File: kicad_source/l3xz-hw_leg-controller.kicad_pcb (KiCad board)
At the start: 2 copper layers, 178 x 29 mm, 57 parts, among them CN1 ARDUINO_NANO_33, CN2 SM04B-SRSS-TB, CN3 SM04B-SRSS-TB, CN4 GH_SM04B-GHS-TB, CN5 GH_SM04B-GHS-TB, CN6 691322310002, CN7 CONN_02X03, CN8 691382010002, U1 AS5048A, U2 AS5048A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

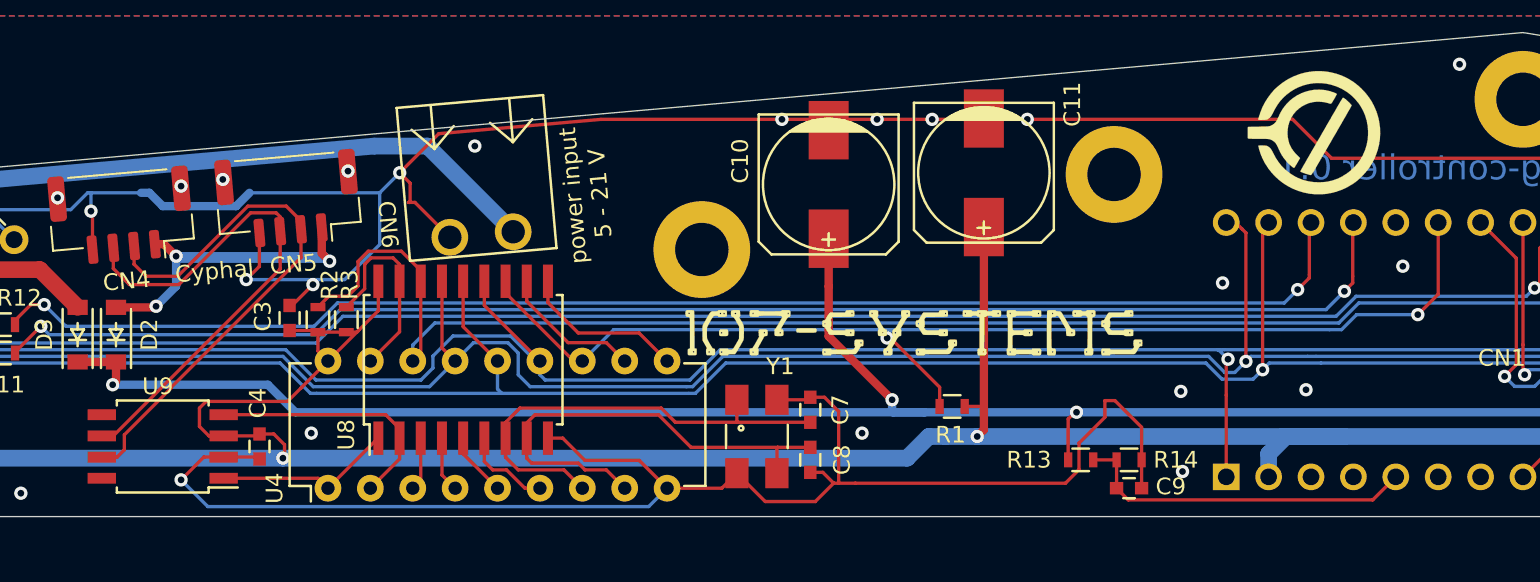
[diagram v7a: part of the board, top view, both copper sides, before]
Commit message: fixed MCP2515_INT and direction label for Arduino
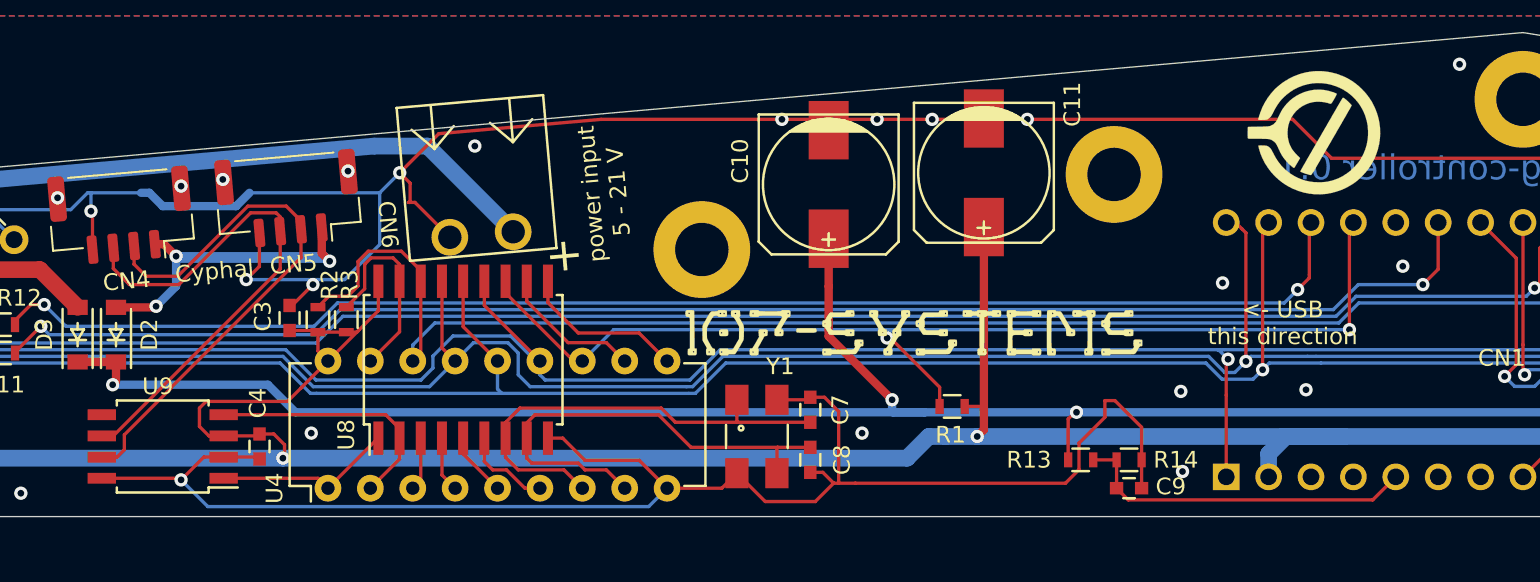
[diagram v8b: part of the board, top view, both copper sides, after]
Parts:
- CN8: value 691382010002 -> WAGO 733-362
- D1: value Led_Small -> LED green
- D2, D3: value DNI -> MBR0530T1G
- D4: value Led_Small -> LED yellow
- D5: value Led_Small -> LED red
- R13: value 10k -> 100k
- R14, R8: value 1k -> 10k
- R15, R16, R5: value 10k -> 3k3
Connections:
- CN1 pad 25: MCP2515_INT -> /SERVO1
- CN1 pad 27: /SERVO1 -> MCP2515_INT
- U9 pad 8: (no net) -> GND
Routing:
- net GND: track 401.6 -> 406.4 mm
- net /SERVO1: track 86.0 -> 90.6 mm
- net MCP2515_INT: track 70.4 -> 66.5 mm
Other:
- board text added: "+"
- board text added: "<- USB this direction"
